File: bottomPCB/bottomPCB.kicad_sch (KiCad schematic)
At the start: 17 parts, among them P1 Pfostenstecker_8_2x4, U1 ESP32-WROOM-32, U2 Pfostenstecker_6_2x3, U3 Switch

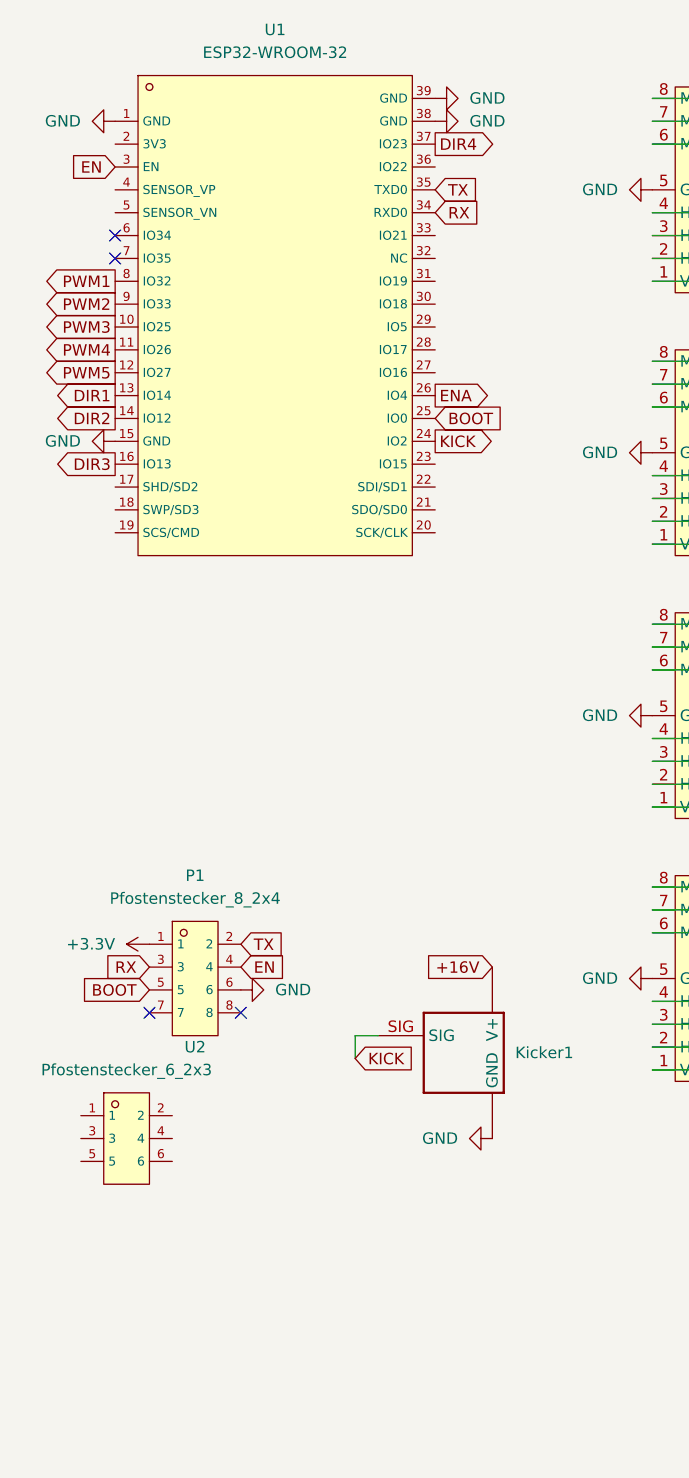
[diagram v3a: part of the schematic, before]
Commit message: added i2c + kicker resistor
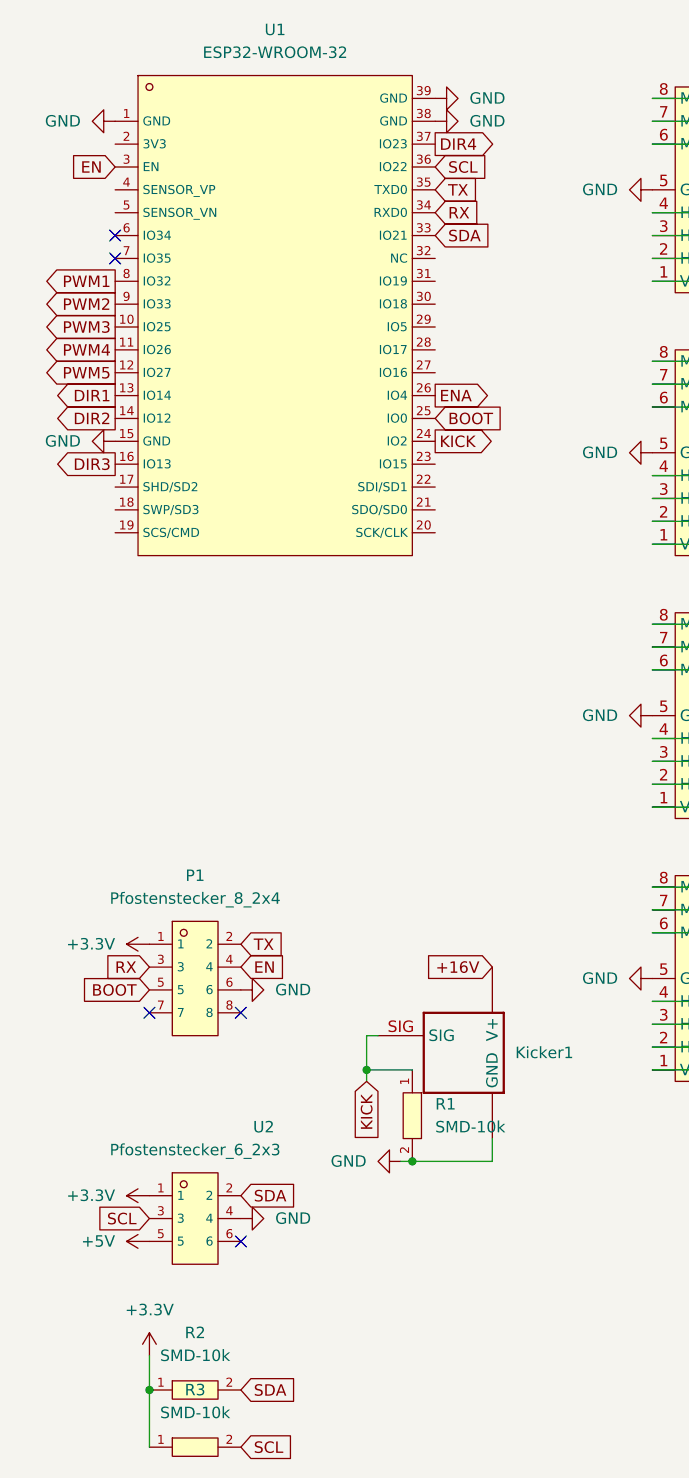
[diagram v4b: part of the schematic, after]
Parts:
- added R1, R2, R3: SMD-10k, BohleBots:R0603, symbol bohlebots.lib:SMD-10k
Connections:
- net +3.3V: now also U2.1, R2.1, R3.1
- net +5V: now also U2.5
- net GND: now also U2.4, R1.2
- net KICK: now also R1.1
- net SDA: now reaches U2.2
- net SDA: now also U1.33 (IO21), R2.2
- net SCL: now reaches U2.3
- net SCL: now also U1.36 (IO22), R3.2
- no-connect marks 8 -> 9
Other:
- moved on the sheet: U2

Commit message: lichtschranke
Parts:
- added R4: SMD-10k, BohleBots:R0603, symbol bohlebots.lib:SMD-10k
- added R5: SMD-100R, BohleBots:R0603, symbol bohlebots.lib:SMD-100R
- added U4, U5: Pinhead_1x02H, BohleBots:HDR-TH_2P-P2.54-H-M-W10.4, symbol bohlebots.lib:Pinhead_1x02H
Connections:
- net +3.3V: now also R4.1, R5.2
- net GND: now also U4.1, U5.1
- net BARRIER: now reaches U1.6 (IO34)
- net BARRIER: now also R4.2, U4.2
- new net: R5.1, U5.2
- no-connect marks 9 -> 8
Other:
- note added: "LED"
- note added: "Lichtschranke"
- note added: "Sensor"
- moved on the sheet: U1

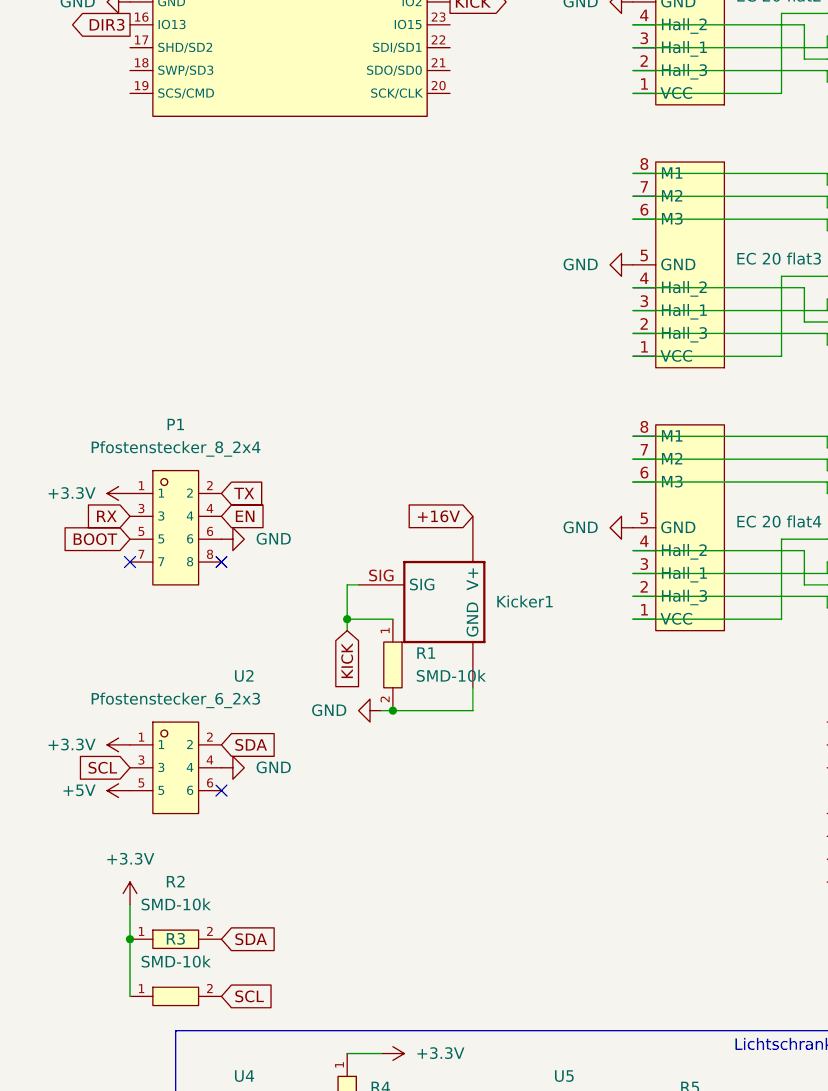
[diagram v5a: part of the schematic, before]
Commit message: added programmer (boot/EN) Resistors + debounce capacitor
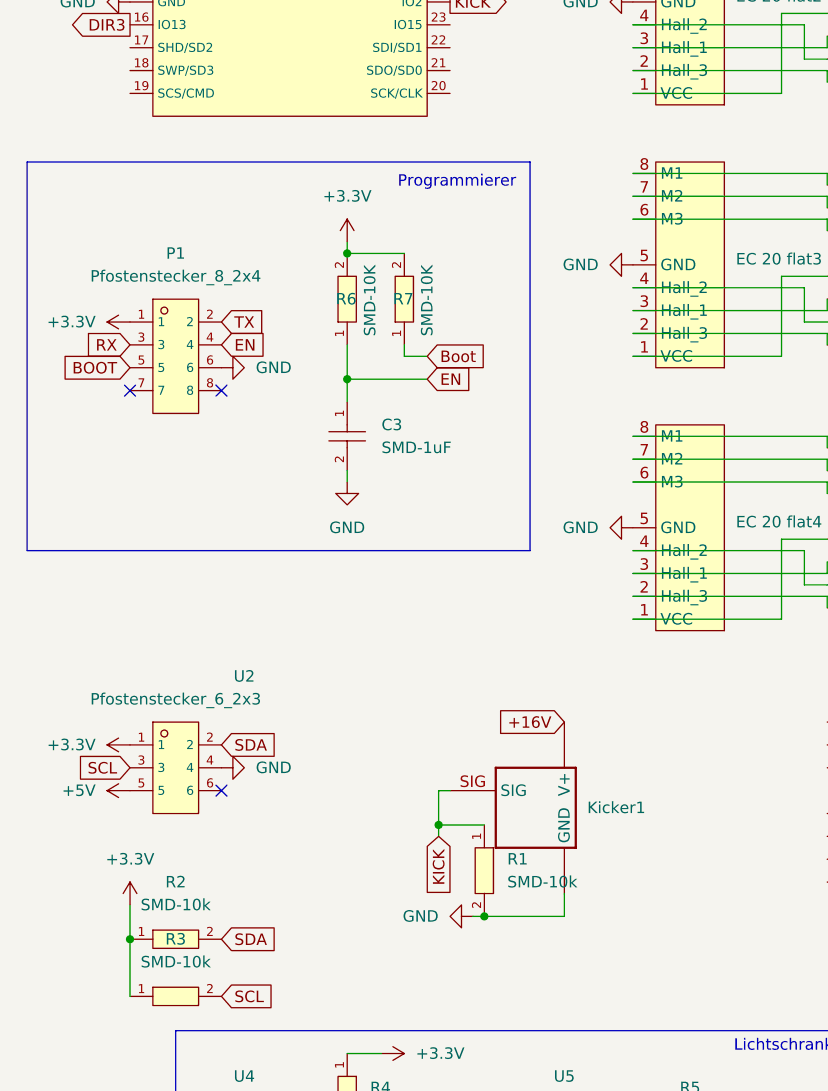
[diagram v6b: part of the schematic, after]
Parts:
- added C3: SMD-1uF, BohleBots:C0603, symbol Bohlebots:SMD-1uF
- added R6, R7: SMD-10K, BohleBots:R0603, symbol Bohlebots:SMD-10k
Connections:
- net +3.3V: now also R6.2, R7.2
- net EN: now also C3.1, R6.1
- net GND: now also C3.2
- new net Boot: R7.1
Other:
- note added: "Programmierer"
- moved on the sheet: Kicker1, P1, R1

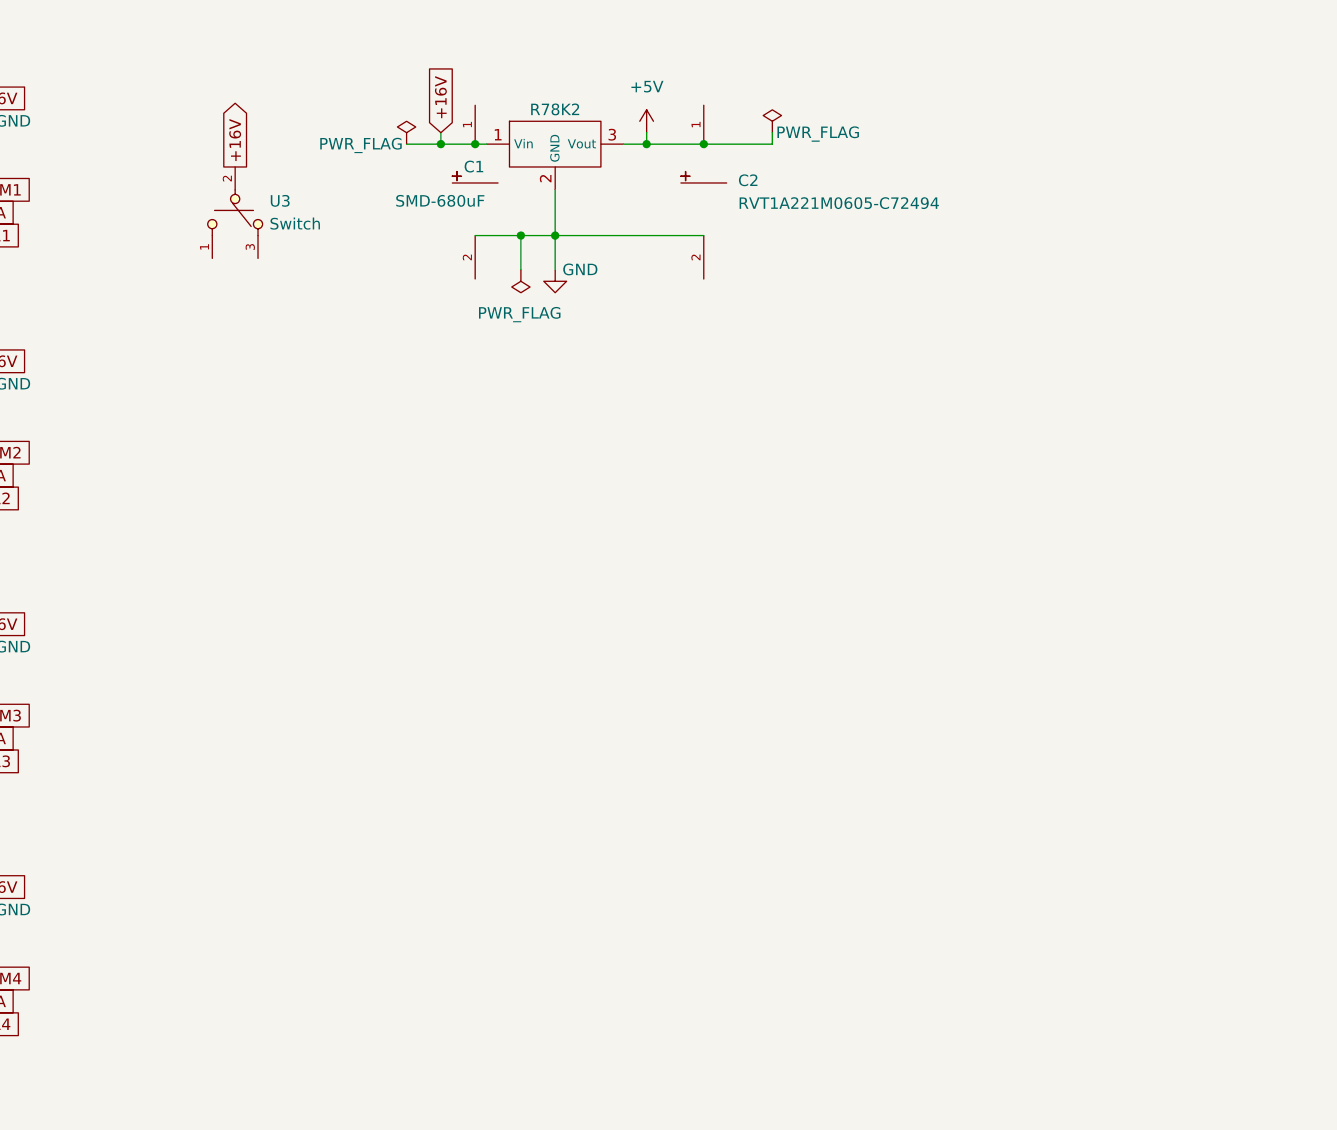
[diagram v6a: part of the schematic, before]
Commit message: added power system + capacitators
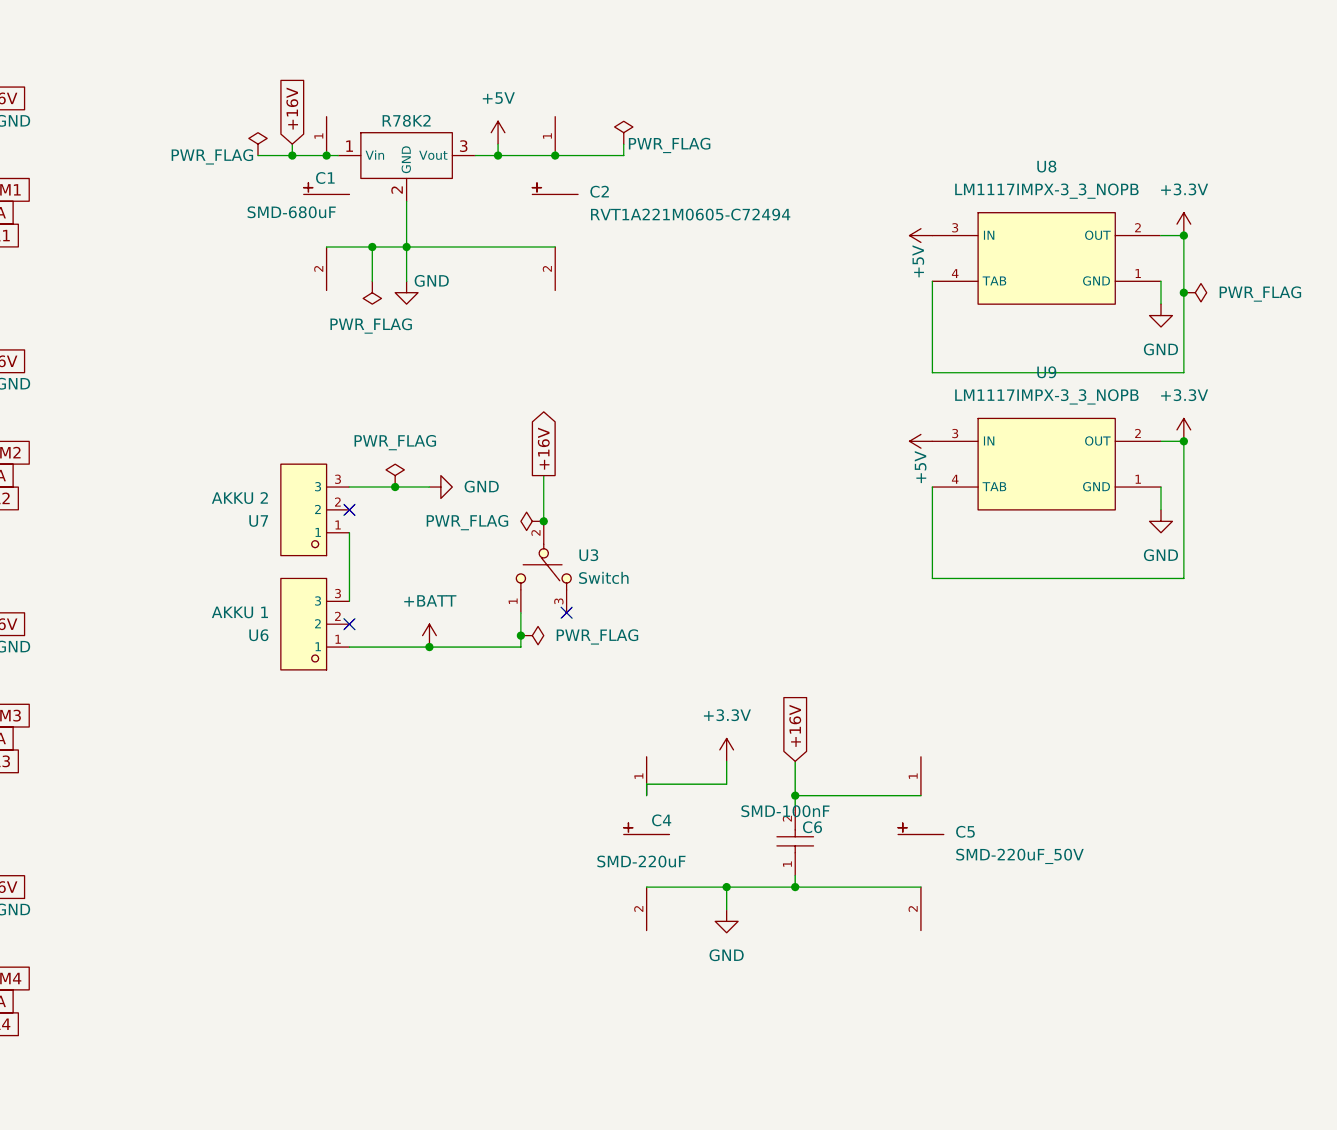
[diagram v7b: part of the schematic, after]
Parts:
- added C4: SMD-220uF, BohleBots:CAP-SMD_BD10.0-L10.3-W10.3-LS11.3-FD, symbol Bohlebots:SMD-220uF_50V
- added C5: SMD-220uF_50V, BohleBots:CAP-SMD_BD10.0-L10.3-W10.3-LS11.3-FD, symbol Bohlebots:SMD-220uF_50V
- added C6: SMD-100nF, BohleBots:C0603, symbol bohlebots.lib:SMD-100nF
- added U6: AKKU 1, BohleBots:CONN-TH_XH-3AW-C722865, symbol bohlebots.lib:XH-3AW_C722865
- added U7: AKKU 2, BohleBots:CONN-TH_XH-3AW-C722865, symbol bohlebots.lib:XH-3AW_C722865
- added U8, U9: LM1117IMPX-3_3_NOPB, BohleBots:SOT-223_L6.5-W3.5-P2.30-LS7.0-BR, symbol Bohlebots:LM1117IMPX-3_3_NOPB
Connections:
- net +16V: now also C5.1, C6.2
- net +3.3V: now also C4.1, U8.2 (OUT), U8.4 (TAB), U9.2 (OUT), U9.4 (TAB)
- net +5V: now also U8.3 (IN), U9.3 (IN)
- net GND: now also C4.2, C5.2, C6.1, U7.3, U8.1 (GND), U9.1 (GND)
- net +BATT: now reaches U3.1
- net +BATT: now also U6.1
- new net: U6.3, U7.1
- no-connect marks 8 -> 11
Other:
- moved on the sheet: C1, C2, R78K2, U3

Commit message: added comments
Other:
- note added: "+3.3V"
- note added: "+5V"
- note added: "ESP32"
- note added: "I2C"
- note added: "Kicker"
- note added: "Motoren"
- moved on the sheet: ESCON-Dribbler, Kicker1, R1, R2, R3, R4, R5, U2, U4, U5, U8, U9
